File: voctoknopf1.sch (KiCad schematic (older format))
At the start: 4 parts

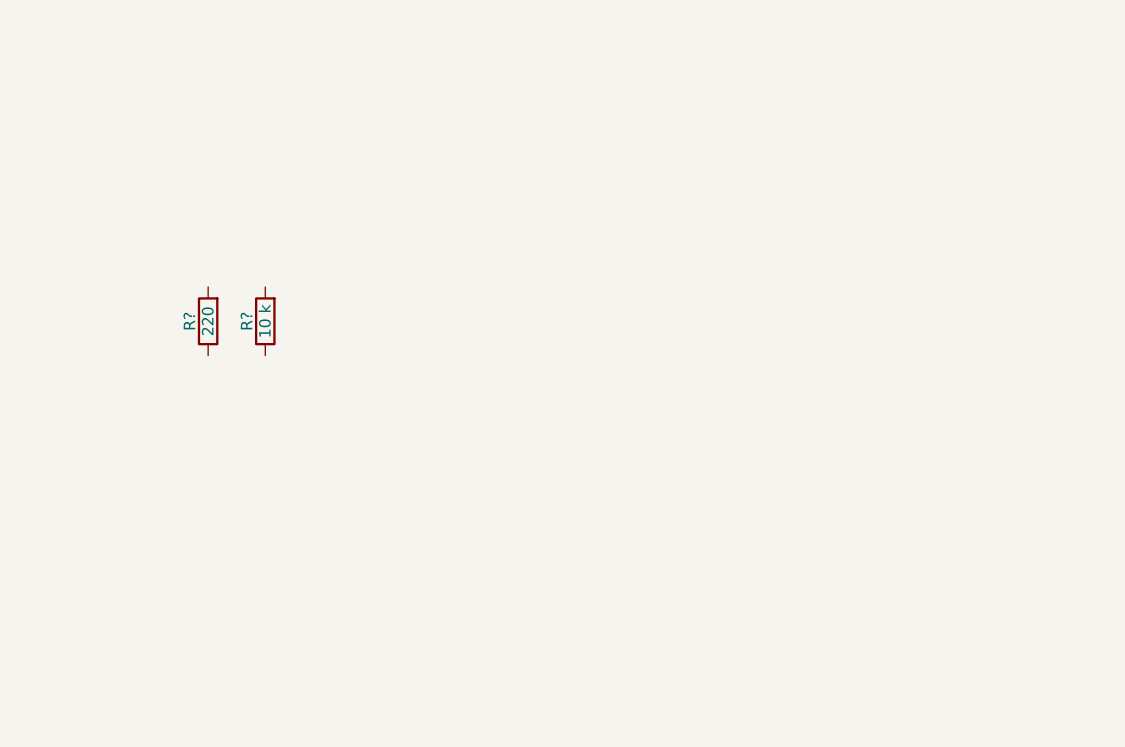
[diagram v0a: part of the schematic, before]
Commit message: 29.11.
erster Versuch mit ethernet shiled und ich habe einen arduino nano für kicad gefunden
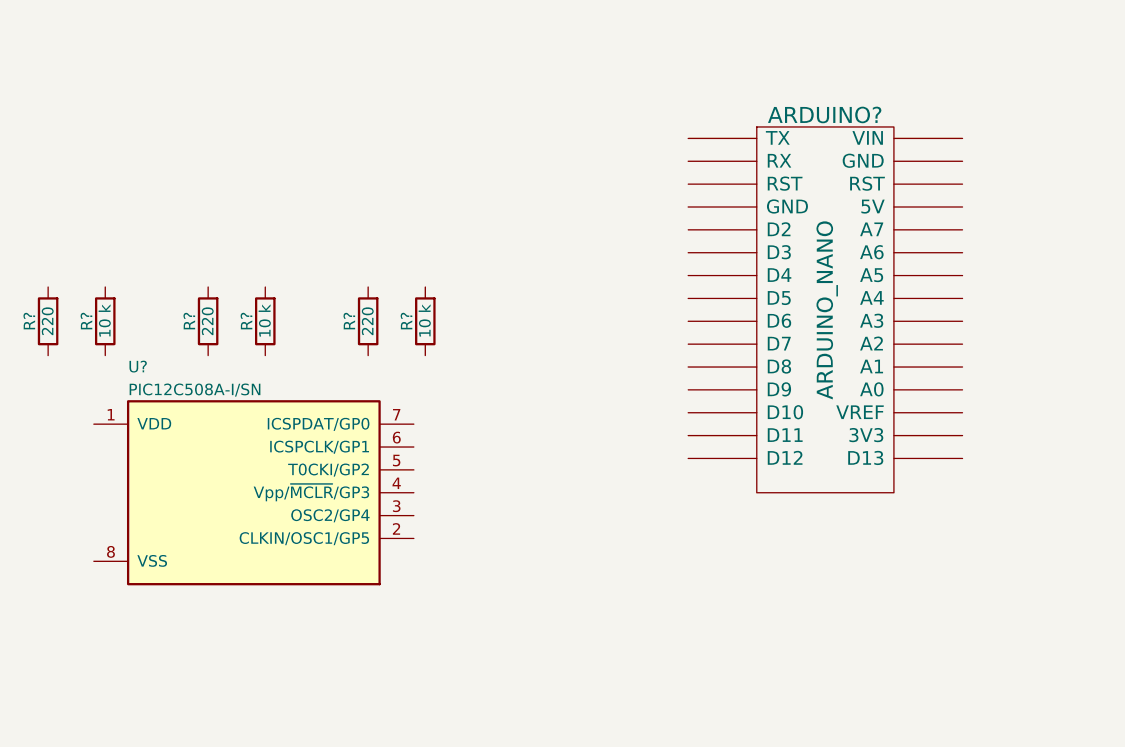
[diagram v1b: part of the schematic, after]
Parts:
- added ARDUINO?: ARDUINO_NANO, symbol ARDUINO_NANO
- added R? (x2): 10 k, symbol R
- added R? (x2): 220, symbol R
- added U?: PIC12C508A-I/SN, symbol PIC12C508A-I/SN
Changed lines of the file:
@@
 LIBS:contrib
 LIBS:valves
+LIBS:arduino
+LIBS:microchip_pic12mcu
 LIBS:voctoknopf1-cache
 EELAYER 25 0
@@
 	1    0    0    -1
 $EndComp
+$Comp
+L R R?
+U 1 1 5A1E8001
+P 4000 2800
+F 0 "R?" V 4080 2800 50  0000 C CNN
+F 1 "10 k" V 4000 2800 50  0000 C CNN
+F 2 "" V 3930 2800 50  0001 C CNN
+F 3 "" H 4000 2800 50  0001 C CNN
+	1    4000 2800
+	-1   0    0    1
+$EndComp
+$Comp
+L R R?
+U 1 1 5A1E8041
+P 3750 2800
+F 0 "R?" V 3830 2800 50  0000 C CNN
+F 1 "220" V 3750 2800 50  0000 C CNN
+F 2 "" V 3680 2800 50  0001 C CNN
+F 3 "" H 3750 2800 50  0001 C CNN
+	1    3750 2800
+	-1   0    0    1
+$EndComp
+$Comp
+L R R?
+U 1 1 5A1E8129
+P 2600 2800
+F 0 "R?" V 2680 2800 50  0000 C CNN
+F 1 "10 k" V 2600 2800 50  0000 C CNN
+F 2 "" V 2530 2800 50  0001 C CNN
+F 3 "" H 2600 2800 50  0001 C CNN
+	1    2600 2800
+	-1   0    0    1
+$EndComp
+$Comp
+L R R?
+U 1 1 5A1E812F
+P 2350 2800
+F 0 "R?" V 2430 2800 50  0000 C CNN
+F 1 "220" V 2350 2800 50  0000 C CNN
+F 2 "" V 2280 2800 50  0001 C CNN
+F 3 "" H 2350 2800 50  0001 C CNN
+	1    2350 2800
+	-1   0    0    1
+$EndComp
+$Comp
+L PIC12C508A-I/SN U?
+U 1 1 5A1E8434
+P 3250 3550
+F 0 "U?" H 2700 4100 50  0000 L CNN
+F 1 "PIC12C508A-I/SN" H 2700 4000 50  0000 L CNN
+F 2 "" H 3250 3550 50  0001 C CNN
+F 3 "" H 3250 3550 50  0001 C CNN
+	1    3250 3550
+	1    0    0    -1
+$EndComp
+$Comp
+L ARDUINO_NANO ARDUINO?
+U 1 1 5A1E84AB
+P 5750 2750
+F 0 "ARDUINO?" H 5750 3600 70  0000 C CNN
+F 1 "ARDUINO_NANO" V 5750 2750 70  0000 C CNN
+F 2 "" H 5750 2750 60  0000 C CNN
+F 3 "" H 5750 2750 60  0000 C CNN
+	1    5750 2750
+	1    0    0    -1
+$EndComp

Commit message: case 3d file, more pcb work
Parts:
- added SW? (x2): MX_D, symbol MX_D
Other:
- moved on the sheet: ARDUINO?, U?
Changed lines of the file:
@@
 LIBS:arduino
 LIBS:microchip_pic12mcu
+LIBS:cherry
+LIBS:keyboard_components
 LIBS:voctoknopf1-cache
 EELAYER 25 0
@@
 L MCP23017 U?
 U 1 1 5A16E83C
-P 7850 2550
-F 0 "U?" H 7750 3575 50  0000 R CNN
-F 1 "MCP23017" H 7750 3500 50  0000 R CNN
-F 2 "" H 7900 1600 50  0001 L CNN
-F 3 "" H 8100 3550 50  0001 C CNN
-	1    7850 2550
+P 7850 2200
+F 0 "U?" H 7750 3225 50  0000 R CNN
+F 1 "MCP23017" H 7750 3150 50  0000 R CNN
+F 2 "" H 7900 1250 50  0001 L CNN
+F 3 "" H 8100 3200 50  0001 C CNN
+	1    7850 2200
 	1    0    0    -1
 $EndComp
@@
 L PIC12C508A-I/SN U?
 U 1 1 5A1E8434
-P 3250 3550
-F 0 "U?" H 2700 4100 50  0000 L CNN
-F 1 "PIC12C508A-I/SN" H 2700 4000 50  0000 L CNN
-F 2 "" H 3250 3550 50  0001 C CNN
-F 3 "" H 3250 3550 50  0001 C CNN
-	1    3250 3550
+P 1500 5500
+F 0 "U?" H 950 6050 50  0000 L CNN
+F 1 "PIC12C508A-I/SN" H 950 5950 50  0000 L CNN
+F 2 "" H 1500 5500 50  0001 C CNN
+F 3 "" H 1500 5500 50  0001 C CNN
+	1    1500 5500
 	1    0    0    -1
 $EndComp
@@
 L ARDUINO_NANO ARDUINO?
 U 1 1 5A1E84AB
-P 5750 2750
-F 0 "ARDUINO?" H 5750 3600 70  0000 C CNN
-F 1 "ARDUINO_NANO" V 5750 2750 70  0000 C CNN
-F 2 "" H 5750 2750 60  0000 C CNN
-F 3 "" H 5750 2750 60  0000 C CNN
-	1    5750 2750
+P 10250 3450
+F 0 "ARDUINO?" H 10250 4300 70  0000 C CNN
+F 1 "ARDUINO_NANO" V 10250 3450 70  0000 C CNN
+F 2 "" H 10250 3450 60  0000 C CNN
+F 3 "" H 10250 3450 60  0000 C CNN
+	1    10250 3450
 	1    0    0    -1
 $EndComp
+$Comp
+L MX_D SW?
+U 1 1 5A1E8A84
+P 5200 1800
+F 0 "SW?" H 5200 1900 60  0000 C CNN
+F 1 "MX_D" H 5200 1800 60  0000 C CNN
+F 2 "" H 5200 1800 60  0001 C CNN
+F 3 "" H 5200 1800 60  0001 C CNN
+	1    5200 1800
+	1    0    0    -1
+$EndComp
+$Comp
+L MX_D SW?
+U 1 1 5A1E8B0E
+P 4150 1850
+F 0 "SW?" H 4150 1950 60  0000 C CNN
+F 1 "MX_D" H 4150 1850 60  0000 C CNN
+F 2 "" H 4150 1850 60  0001 C CNN
+F 3 "" H 4150 1850 60  0001 C CNN
+	1    4150 1850
+	1    0    0    -1
+$EndComp

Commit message: pcb weiter machen
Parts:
- removed U?: PIC12C508A-I/SN, symbol PIC12C508A-I/SN
- added ARDUINO1: ARDUINO_NANO, symbol ARDUINO_NANO
- added R? (x9): 10 k, symbol R
- added R? (x9): 220, symbol R
- added SW? (x10): MX_D, symbol MX_D
- ARDUINO2: renamed from ARDUINO?; value ARDUINO_NANO -> Nano Ethernet Shield
- gave numbers to parts that had none: 10
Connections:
- wire segments 0 -> 43
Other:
- moved on the sheet: ARDUINO2, R1, R2, R3, R4, R5, R6, SW1, SW2, U2, U3

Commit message: more pcb foo
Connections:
- net labels added: 5V, GND
- wire segments 43 -> 185
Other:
- moved on the sheet: R1, R2, R3, R4, R5, R6, R?, SW1, SW2, SW?, U2, U3

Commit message: more pcb
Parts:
- gave numbers to parts that had none: 1
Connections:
- net 5V: now also SW?.1 (A), SW?.1 (A), SW?.1 (A), SW?.1 (A), SW?.1 (A)
- net GND: now also R?.1, R?.1, R?.1, R?.1, R?.1, SW?.4 (D), SW?.4 (D), SW?.4 (D), SW?.4 (D), SW?.4 (D)
- net at R?.2, SW?.2 (B): now also U2.7 (GPB6); no longer U2.21 (GPA0)
- net at U2.22 (GPA1): now also R?.1; no longer R?.1
- net at R?.2, SW?.2 (B): now also U2.21 (GPA0); no longer U2.23 (GPA2)
- net at U2.24 (GPA3): now also R?.1; no longer R?.1
- net at R?.2, SW?.2 (B): now also U2.23 (GPA2); no longer U2.25 (GPA4)
- net at U2.26 (GPA5): now also R?.1; no longer R?.1
- net at R?.2, SW?.2 (B): now also U2.25 (GPA4); no longer U2.27 (GPA6)
- net at U2.28 (GPA7): no longer R?.1
- net at U2.8 (GPB7): now also R?.1
- net at U3.1 (GPB0): now also R?.2, SW?.2 (B)
- net at U3.2 (GPB1): now also R?.1
- net at U3.21 (GPA0): now also R?.2, SW?.2 (B)
- net at U3.22 (GPA1): now also R?.2
- net at U3.3 (GPB2): now also R?.2, SW?.2 (B)
- net at U3.4 (GPB3): now also R?.1
- net at U3.5 (GPB4): now also R?.2, SW?.2 (B)
- net at U3.6 (GPB5): now also R?.1
- net at U3.7 (GPB6): now also R?.2, SW?.2 (B)
- net at U3.8 (GPB7): now also R?.1
- net at R?.2: now also SW?.3 (B) (x4)
- net at R?.1: now also SW?.3 (B)
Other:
- moved on the sheet: R?, SW?, U3

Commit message: PCB und Grafiken
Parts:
- added D? (x2): LED, symbol LED
- added J?: Conn_01x02, symbol Conn_01x02
- added R?: 10 k, symbol R
- added R? (x2): 220, symbol R
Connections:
- net 5V: now also U3.15 (A0), U3.18 (~RESET), U3.9 (VCC), J?.1 (Pin_1)
- net GND: now also U3.10 (GND), U3.16 (A1), U3.17 (A2), D?.1 (K), D?.1 (K), R?.1
- net at ARDUINO1.24 (A5), U2.12 (SCL): now also U3.12 (SCL)
- net at ARDUINO1.23 (A4), U2.13 (SDA): now also U3.13 (SDA)
- net at ARDUINO1.10 (D7): now also R?.1
- net at ARDUINO1.8 (D5): now also J?.2 (Pin_2), R?.2
- net at ARDUINO1.9 (D6): now also R?.1
- new net: D?.2 (A), R?.2 (x2)
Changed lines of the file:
@@
 Text Label 3450 700  0    60   ~ 0
 GND
-Text Label 5800 3550 0    60   ~ 0
+Text Label 5800 3600 0    60   ~ 0
 5V
 Text Label 3250 3900 0    60   ~ 0
@@
 Text Label 1350 5600 0    60   ~ 0
 GND
+Text Label 1350 2500 0    60   ~ 0
+5V
+Text Label 1250 2250 0    60   ~ 0
+GND
+$Comp
+L LED D?
+U 1 1 5A2062E7
+P 8850 1400
+F 0 "D?" H 8850 1500 50  0000 C CNN
+F 1 "LED" H 8850 1300 50  0000 C CNN
+F 2 "" H 8850 1400 50  0001 C CNN
+F 3 "" H 8850 1400 50  0001 C CNN
+	1    8850 1400
+	0    1    1    0
+$EndComp
+$Comp
+L LED D?
+U 1 1 5A2063A3
+P 8450 1400
+F 0 "D?" H 8450 1500 50  0000 C CNN
+F 1 "LED" H 8450 1300 50  0000 C CNN
+F 2 "" H 8450 1400 50  0001 C CNN
+F 3 "" H 8450 1400 50  0001 C CNN
+	1    8450 1400
+	0    1    1    0
+$EndComp
+$Comp
+L R R?
+U 1 1 5A2069C6
+P 9200 2950
+F 0 "R?" V 9280 2950 50  0000 C CNN
+F 1 "10 k" V 9200 2950 50  0000 C CNN
+F 2 "" V 9130 2950 50  0001 C CNN
+F 3 "" H 9200 2950 50  0001 C CNN
+	1    9200 2950
+	-1   0    0    1
+$EndComp
+$Comp
+L R R?
+U 1 1 5A2069CC
+P 8850 1850
+F 0 "R?" V 8930 1850 50  0000 C CNN
+F 1 "220" V 8850 1850 50  0000 C CNN
+F 2 "" V 8780 1850 50  0001 C CNN
+F 3 "" H 8850 1850 50  0001 C CNN
+	1    8850 1850
+	-1   0    0    1
+$EndComp
+$Comp
+L R R?
+U 1 1 5A2083E1
+P 8450 1850
+F 0 "R?" V 8530 1850 50  0000 C CNN
+F 1 "220" V 8450 1850 50  0000 C CNN
+F 2 "" V 8380 1850 50  0001 C CNN
+F 3 "" H 8450 1850 50  0001 C CNN
+	1    8450 1850
+	-1   0    0    1
+$EndComp
+$Comp
+L Conn_01x02 J?
+U 1 1 5A20964F
+P 9400 1500
+F 0 "J?" H 9400 1600 50  0000 C CNN
+F 1 "Conn_01x02" H 9400 1300 50  0000 C CNN
+F 2 "" H 9400 1500 50  0001 C CNN
+F 3 "" H 9400 1500 50  0001 C CNN
+	1    9400 1500
+	1    0    0    -1
+$EndComp
 Wire Wire Line
 	3850 3900 600  3900
@@
 	1650 1450 1650 1750
 Wire Wire Line
-	1250 700  6600 700
+	1250 700  8850 700
 Wire Wire Line
 	1250 700  1250 1450
@@
 	6050 3200 6050 1100
 Wire Wire Line
-	3850 3200 6600 3200
+	3850 3200 9200 3200
 Wire Wire Line
 	6050 1100 6600 1100
@@
 	6800 800  6800 1250
 Wire Wire Line
-	1350 800  6800 800
+	1350 800  9200 800
 Wire Wire Line
 	1350 800  1350 1200
@@
 Connection ~ 1750 2500
 Wire Wire Line
-	2450 2550 2450 2500
+	2450 2500 2450 2550
 Connection ~ 2450 2500
 Wire Wire Line
-	3250 2550 3250 2500
+	3250 2500 3250 2550
 Connection ~ 3250 2500
 Wire Wire Line
@@
 Connection ~ 6050 2550
 Wire Wire Line
-	5700 2250 5700 1150
+	5700 1150 5700 4200
 Wire Wire Line
 	5700 1150 7100 1150
@@
 	5500 2350 5750 2350
 Wire Wire Line
-	5750 2350 5750 1200
+	5750 4300 5750 1200
 Wire Wire Line
 	5750 1200 7200 1200
@@
 Wire Wire Line
 	3150 4600 3150 5000
-Wire Wire Line
-	2400 4600 2400 5000
 Wire Wire Line
 	1700 4600 1700 5000
@@
 Connection ~ 1950 4800
 Wire Wire Line
-	2650 4500 2650 5000
-Wire Wire Line
 	2650 4500 2400 4500
-Connection ~ 2650 4850
 Wire Wire Line
 	3400 4500 3400 5000
@@
 Wire Wire Line
 	3550 4950 3550 4850
-Wire Wire Line
-	3550 4850 2650 4850
 Wire Wire Line
 	3500 5150 4250 5150
@@
 	4200 2450 4500 2450
 Wire Wire Line
-	3050 4050 3050 2500
+	3050 2500 3050 4050
 Connection ~ 3050 2500
 Connection ~ 3050 4050
 Wire Wire Line
-	3250 2500 1050 2500
-Text Label 1350 2500 0    60   ~ 0
-5V
+	1050 2500 3250 2500
 Wire Wire Line
 	4250 2550 4500 2550
-Text Label 1250 2250 0    60   ~ 0
-GND
 Wire Wire Line
 	2950 6000 2950 5600
 Connection ~ 2950 5600
+Wire Wire Line
+	2650 4500 2650 5000
+Wire Wire Line
+	2400 4600 2400 5000
+Wire Wire Line
+	3550 4850 2650 4850
+Connection ~ 2650 4850
+Wire Wire Line
+	4750 4350 4700 4350
+Wire Wire Line
+	4700 4350 4700 4050
+Connection ~ 4700 4050
+Wire Wire Line
+	4750 6350 4750 6550
+Wire Wire Line
+	4750 6550 2400 6550
+Wire Wire Line
+	2400 6550 2400 5600
+Connection ~ 2400 5600
+Wire Wire Line
+	5250 5950 5300 5950
+Wire Wire Line
+	5300 5950 5300 4050
+Connection ~ 5300 4050
+Wire Wire Line
+	5250 6050 5350 6050
+Wire Wire Line
+	5350 3200 5350 6150
+Connection ~ 5350 3200
+Wire Wire Line
+	5350 6150 5250 6150
+Connection ~ 5350 6050
+Wire Wire Line
+	5250 5650 5400 5650
+Wire Wire Line
+	5400 5650 5400 4200
+Wire Wire Line
+	5400 4200 5700 4200
+Connection ~ 5700 2250
+Wire Wire Line
+	5250 5750 5450 5750
+Wire Wire Line
+	5450 5750 5450 4300
+Wire Wire Line
+	5450 4300 5750 4300
+Connection ~ 5750 2350
+Wire Wire Line
+	5250 4550 5300 4550
+Connection ~ 5300 4550
+Wire Wire Line
+	8450 700  8450 1250
+Connection ~ 6600 700
+Wire Wire Line
+	8850 700  8850 1250
+Connection ~ 8450 700
+Wire Wire Line
+	8450 1700 8450 1550
+Wire Wire Line
+	8850 1700 8850 1550
+Wire Wire Line
+	7400 2450 7400 2650
+Wire Wire Line
+	7400 2650 8450 2650
+Wire Wire Line
+	8450 2650 8450 2000
+Wire Wire Line
+	7300 2450 7300 2700
+Wire Wire Line
+	7300 2700 8850 2700
+Wire Wire Line
+	8850 2700 8850 2000
+Wire Wire Line
+	7200 2450 7200 2800
+Wire Wire Line
+	7200 2800 9200 2800
+Connection ~ 6800 800
+Wire Wire Line
+	9200 3200 9200 3100
+Connection ~ 6600 3200
+Wire Wire Line
+	9200 800  9200 1500
+Wire Wire Line
+	9200 2800 9200 1600
 $EndSCHEMATC
